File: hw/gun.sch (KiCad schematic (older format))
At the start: 1 part, among them J9 IDC_02X05

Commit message: updated schematic
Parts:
- J9: footprint Connectors:IDC_Header_Straight_10pins -> Connector_IDC:IDC-Header_2x05_P2.54mm_Vertical
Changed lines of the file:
@@
 F 0 "J9" H 4000 3192 50  0000 C CNN
 F 1 "IDC_02X05" H 4000 3101 50  0000 C CNN
-F 2 "Connectors:IDC_Header_Straight_10pins" V 4550 2750 50  0001 C CNN
+F 2 "Connector_IDC:IDC-Header_2x05_P2.54mm_Vertical" V 4550 2750 50  0001 C CNN
 F 3 "~" V 4500 2750 50  0001 C CNN
 	1    4000 2750

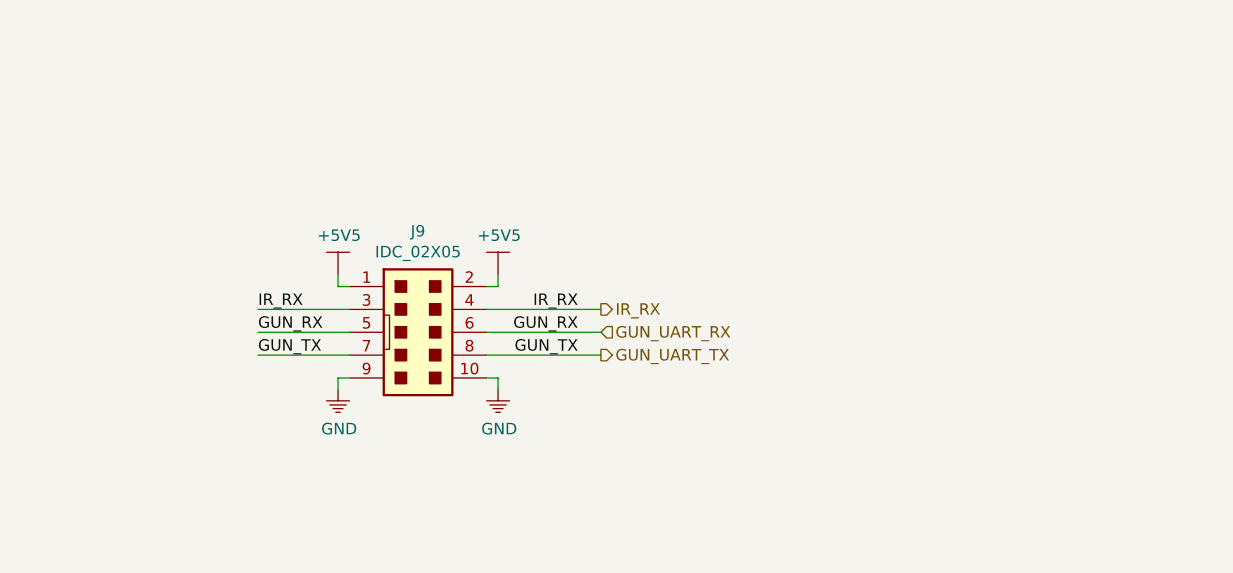
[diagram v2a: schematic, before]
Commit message: updated schematic added buffer to gun uart and updated pcb
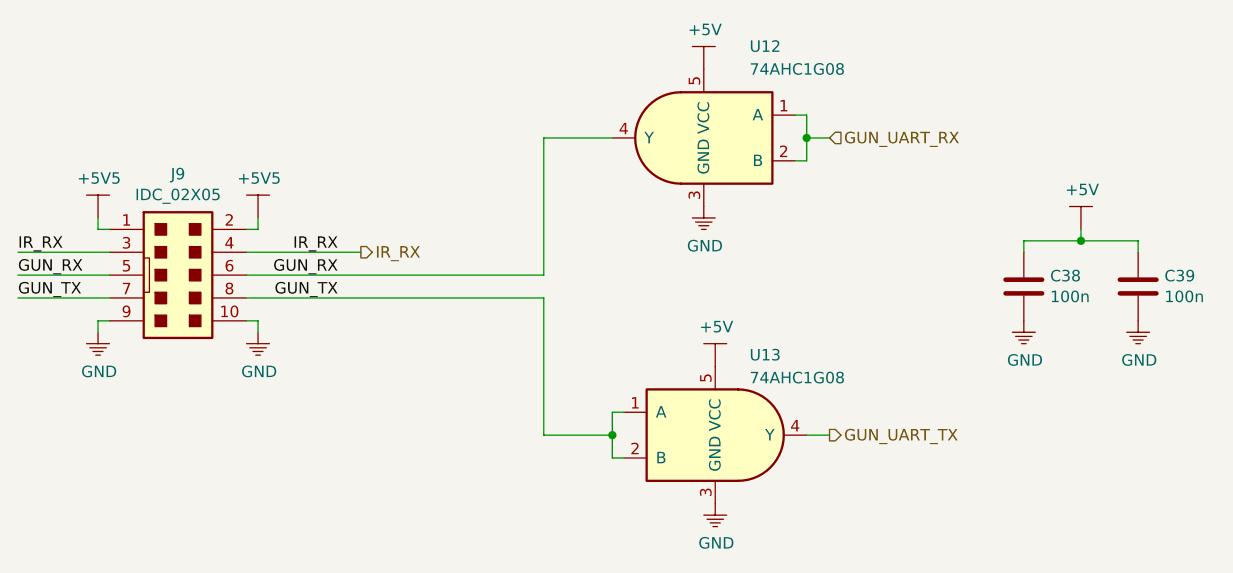
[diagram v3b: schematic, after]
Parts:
- added C38, C39: 100n, Capacitor_SMD:C_0805_2012Metric, symbol Device:C
- added U12, U13: 74AHC1G08, Package_TO_SOT_SMD:SOT-23-5, symbol KLIB_Logic:74AHC1G08
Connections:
- net GND: now also C38.2, C39.2, U12.3 (GND), U13.3 (GND)
- net GUN_UART_RX: now also U12.1 (A), U12.2 (B); no longer J9.5, J9.6
- net GUN_UART_TX: now also U13.4 (Y); no longer J9.7, J9.8
- new net +5V: C38.1, C39.1, U12.5 (VCC), U13.5 (VCC)
- new net GUN_RX: J9.5, J9.6, U12.4 (Y)
- new net GUN_TX: J9.7, J9.8, U13.1 (A), U13.2 (B)
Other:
- moved on the sheet: J9
